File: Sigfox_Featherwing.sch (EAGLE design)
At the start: 14 parts, among them U1 RC1692, X1 SMA-SMD

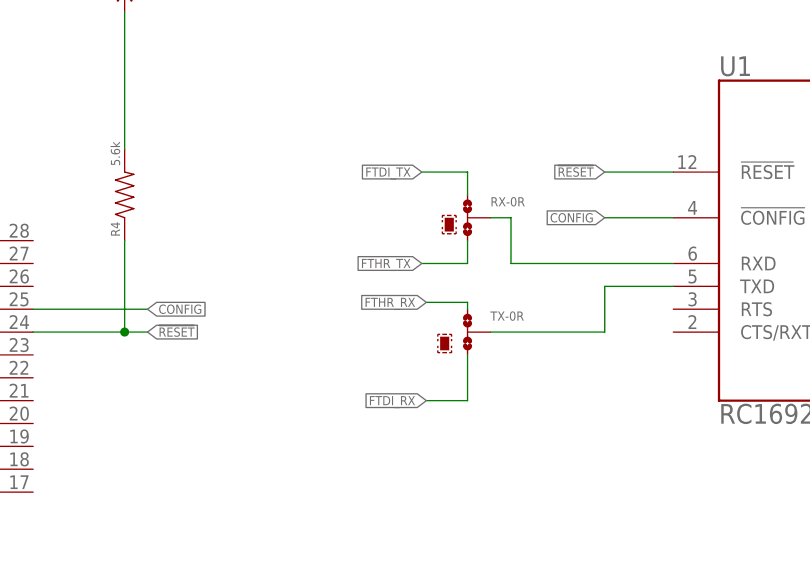
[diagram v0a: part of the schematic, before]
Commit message: CHanging RX and TX lines on sigfox board
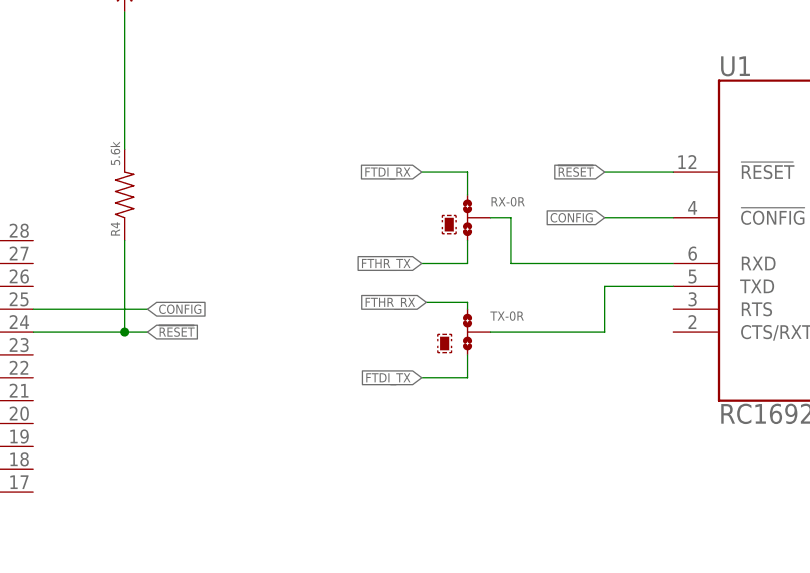
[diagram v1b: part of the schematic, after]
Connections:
- net FTDI_RX: now also RX-0R.1; no longer TX-0R.3
- net FTDI_TX: now also TX-0R.3; no longer RX-0R.1
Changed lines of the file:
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@@
 <?xml version="1.0" encoding="utf-8"?>
 <!DOCTYPE eagle SYSTEM "eagle.dtd">
-<eagle version="9.5.0">
+<eagle version="9.4.1">
 <drawing>
 <settings>
@@
 </segment>
 <segment>
+<pinref part="TX" gate="-0R" pin="3"/>
+<wire x1="147.32" y1="104.14" x2="147.32" y2="101.6" width="0.1524" layer="91"/>
+<wire x1="147.32" y1="101.6" x2="142.24" y2="101.6" width="0.1524" layer="91"/>
+<label x="142.24" y="101.6" size="1.016" layer="95" font="vector" ratio="20" rot="R180" xref="yes"/>
+</segment>
+</net>
+<net name="FTDI_RX" class="0">
+<segment>
+<pinref part="J1" gate="G$1" pin="RXI"/>
+<wire x1="185.42" y1="63.5" x2="190.5" y2="63.5" width="0.1524" layer="91"/>
+<label x="190.5" y="63.5" size="1.016" layer="95" font="vector" ratio="20" xref="yes"/>
+</segment>
+<segment>
 <pinref part="RX" gate="-0R" pin="1"/>
 <wire x1="147.32" y1="121.92" x2="147.32" y2="124.46" width="0.1524" layer="91"/>
@@
 </segment>
 </net>
-<net name="FTDI_RX" class="0">
-<segment>
-<pinref part="J1" gate="G$1" pin="RXI"/>
-<wire x1="185.42" y1="63.5" x2="190.5" y2="63.5" width="0.1524" layer="91"/>
-<label x="190.5" y="63.5" size="1.016" layer="95" font="vector" ratio="20" xref="yes"/>
-</segment>
-<segment>
-<pinref part="TX" gate="-0R" pin="3"/>
-<wire x1="147.32" y1="104.14" x2="147.32" y2="99.06" width="0.1524" layer="91"/>
-<wire x1="147.32" y1="99.06" x2="142.748" y2="99.06" width="0.1524" layer="91"/>
-<label x="142.748" y="99.06" size="1.016" layer="95" font="vector" ratio="20" rot="R180" xref="yes"/>
-</segment>
-</net>
